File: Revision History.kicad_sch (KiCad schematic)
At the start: 0 parts

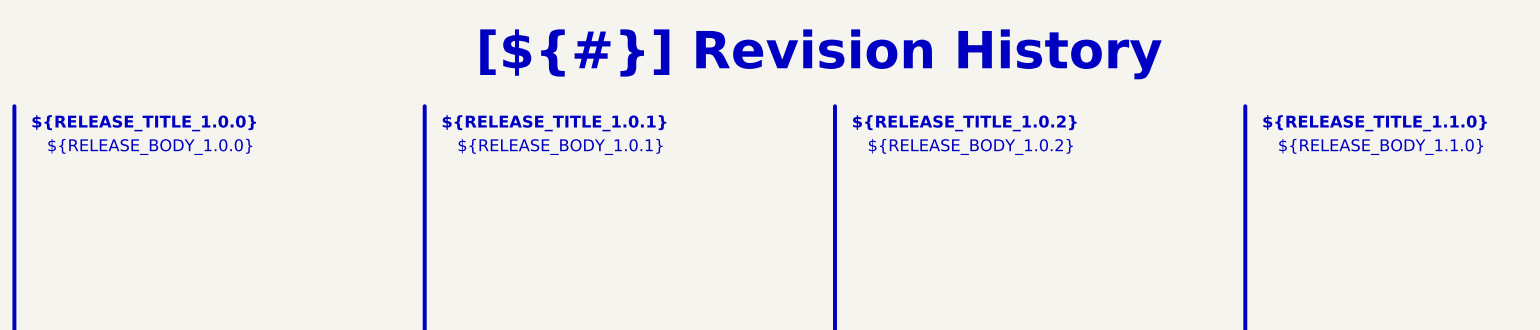
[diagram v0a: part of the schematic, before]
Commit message: Fill template pages: block diagram, power sequencing, cover notes, architecture
- Block Diagram redrawn from the real design: phase path (MR60PW, shunts),
  current and voltage channels with their gains and bandwidths, AD7606C-18,
  power chain, target specifications
- Power - Sequencing: start-up curves taken from the LTspice simulations
  (boost soft-start, analog rails) and rail table with sources, levels
  and timings
- Cover page: real design notes instead of the template examples
- Project Architecture: power-supply block documented, contiguous page
  numbers (Power Supply is page 6)
- Revision History: one column fed by the [Unreleased] changelog section
- sheet titles shortened so they fit the cover-page index: INA241 - Phase
  Sensing, Power Supply - Analog Rails

Sheet-level polylines carry no fill attribute (KiBot schematic reader).

Co-Authored-By: Claude Opus 5.5 <noreply@anthropic.com>
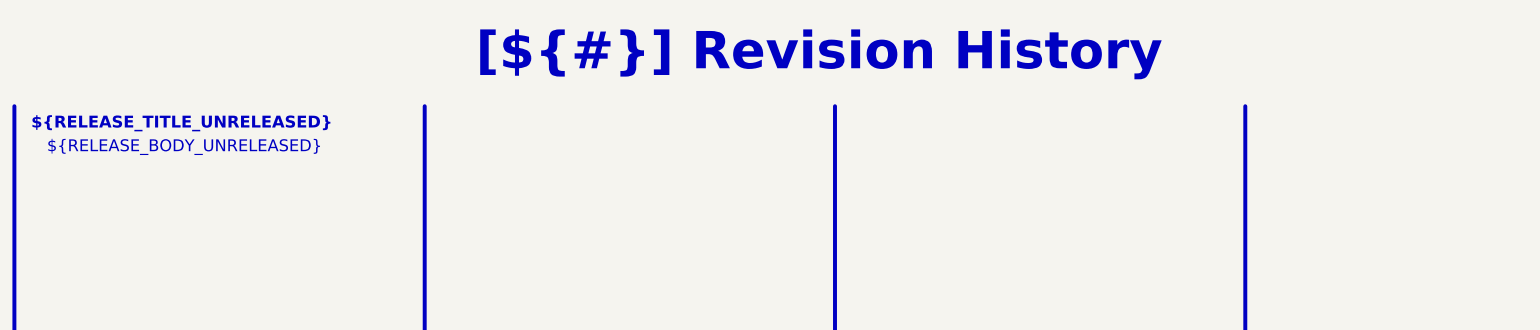
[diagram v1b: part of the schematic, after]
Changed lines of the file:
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@@
 		(company "${COMPANY}")
-	)
-	(text_box "${RELEASE_BODY_1.1.0}"
-		(exclude_from_sim no)
-		(at 220.98 35.56 0)
-		(size 58.42 111.76)
-		(margins 1.4287 1.4287 1.4287 1.4287)
-		(stroke
-			(width -0.0001)
-			(type default)
-		)
-		(fill
-			(type none)
-		)
-		(effects
-			(font
-				(face "Arial")
-				(size 1.905 1.905)
-				(color 0 0 0 1)
-			)
-			(justify left top)
-		)
 	)
 	(text_box "[${#}] ${TITLE}"
@@
 		)
 	)
-	(text_box "${RELEASE_BODY_1.0.0}"
+	(text_box "${RELEASE_BODY_UNRELEASED}"
 		(exclude_from_sim no)
 		(at 22.86 35.56 0)
@@
 		)
 	)
-	(text_box "${RELEASE_TITLE_1.0.2}"
-		(exclude_from_sim no)
-		(at 152.4 31.75 0)
-		(size 57.15 7.62)
-		(margins 1.4287 1.4287 1.4287 1.4287)
-		(stroke
-			(width -0.0001)
-			(type default)
-		)
-		(fill
-			(type none)
-		)
-		(effects
-			(font
-				(face "Arial")
-				(size 1.905 1.905)
-				(thickness 0.254)
-				(bold yes)
-			)
-			(justify left top)
-		)
-	)
-	(text_box "${RELEASE_BODY_1.0.2}"
-		(exclude_from_sim no)
-		(at 154.94 35.56 0)
-		(size 58.42 111.76)
-		(margins 1.4287 1.4287 1.4287 1.4287)
-		(stroke
-			(width -0.0001)
-			(type default)
-		)
-		(fill
-			(type none)
-		)
-		(effects
-			(font
-				(face "Arial")
-				(size 1.905 1.905)
-				(color 0 0 0 1)
-			)
-			(justify left top)
-		)
-	)
-	(text_box "${RELEASE_BODY_1.0.1}"
-		(exclude_from_sim no)
-		(at 88.9 35.56 0)
-		(size 57.15 105.41)
-		(margins 1.4287 1.4287 1.4287 1.4287)
-		(stroke
-			(width -0.0001)
-			(type default)
-		)
-		(fill
-			(type none)
-		)
-		(effects
-			(font
-				(face "Arial")
-				(size 1.905 1.905)
-				(color 0 0 0 1)
-			)
-			(justify left top)
-		)
-	)
-	(text_box "${RELEASE_TITLE_1.0.0}"
+	(text_box "${RELEASE_TITLE_UNRELEASED}"
 		(exclude_from_sim no)
 		(at 20.32 31.75 0)
 		(size 57.15 7.62)
 		(margins 1.4287 1.4287 1.4287 1.4287)
-		(stroke
-			(width -0.0001)
-			(type default)
-		)
-		(fill
-			(type none)
-		)
-		(effects
-			(font
-				(face "Arial")
-				(size 1.905 1.905)
-				(thickness 0.254)
-				(bold yes)
-			)
-			(justify left top)
-		)
-	)
-	(text_box "${RELEASE_TITLE_1.0.1}"
-		(exclude_from_sim no)
-		(at 86.36 31.75 0)
-		(size 57.15 7.62)
-		(margins 1.4287 1.4287 1.4287 1.4287)
-		(stroke
-			(width -0.0001)
-			(type default)
-		)
-		(fill
-			(type none)
-		)
-		(effects
-			(font
-				(face "Arial")
-				(size 1.905 1.905)
-				(thickness 0.254)
-				(bold yes)
-			)
-			(justify left top)
-		)
-	)
-	(text_box "${RELEASE_TITLE_1.1.0}"
-		(exclude_from_sim no)
-		(at 218.44 31.75 0)
-		(size 57.15 7.62)
-		(margins 1.4287 1.4287 1.4287 1.4287)

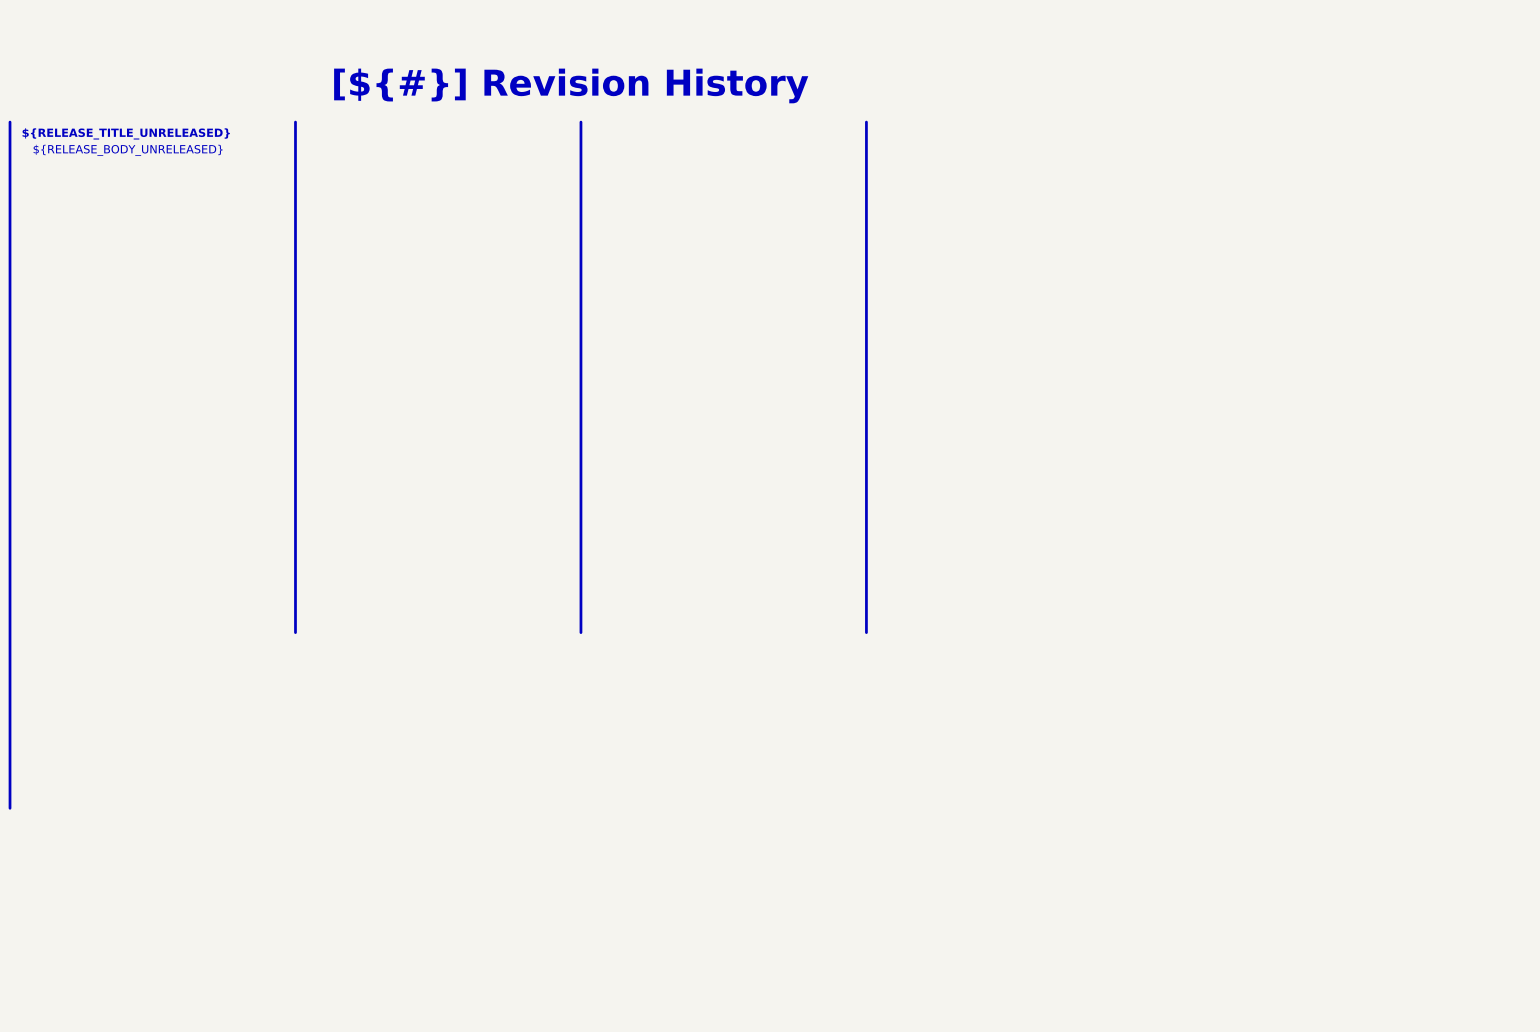
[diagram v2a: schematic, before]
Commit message: Restyle schematic sheets, new title block logo, WE-MAPI inductor in simulations
- Schematic sheets: restyled frames, tables and text boxes
- Title block: INGENIERIE FRANCE logo in KDT_Template_GIT.kicad_wks
- LTspice: L1 modelled as WE-MAPI 4030 74438357022 (22 mOhm),
  simulations 01 and 03 rerun, README and results updated

Co-Authored-By: Claude Opus 5.5 <noreply@anthropic.com>
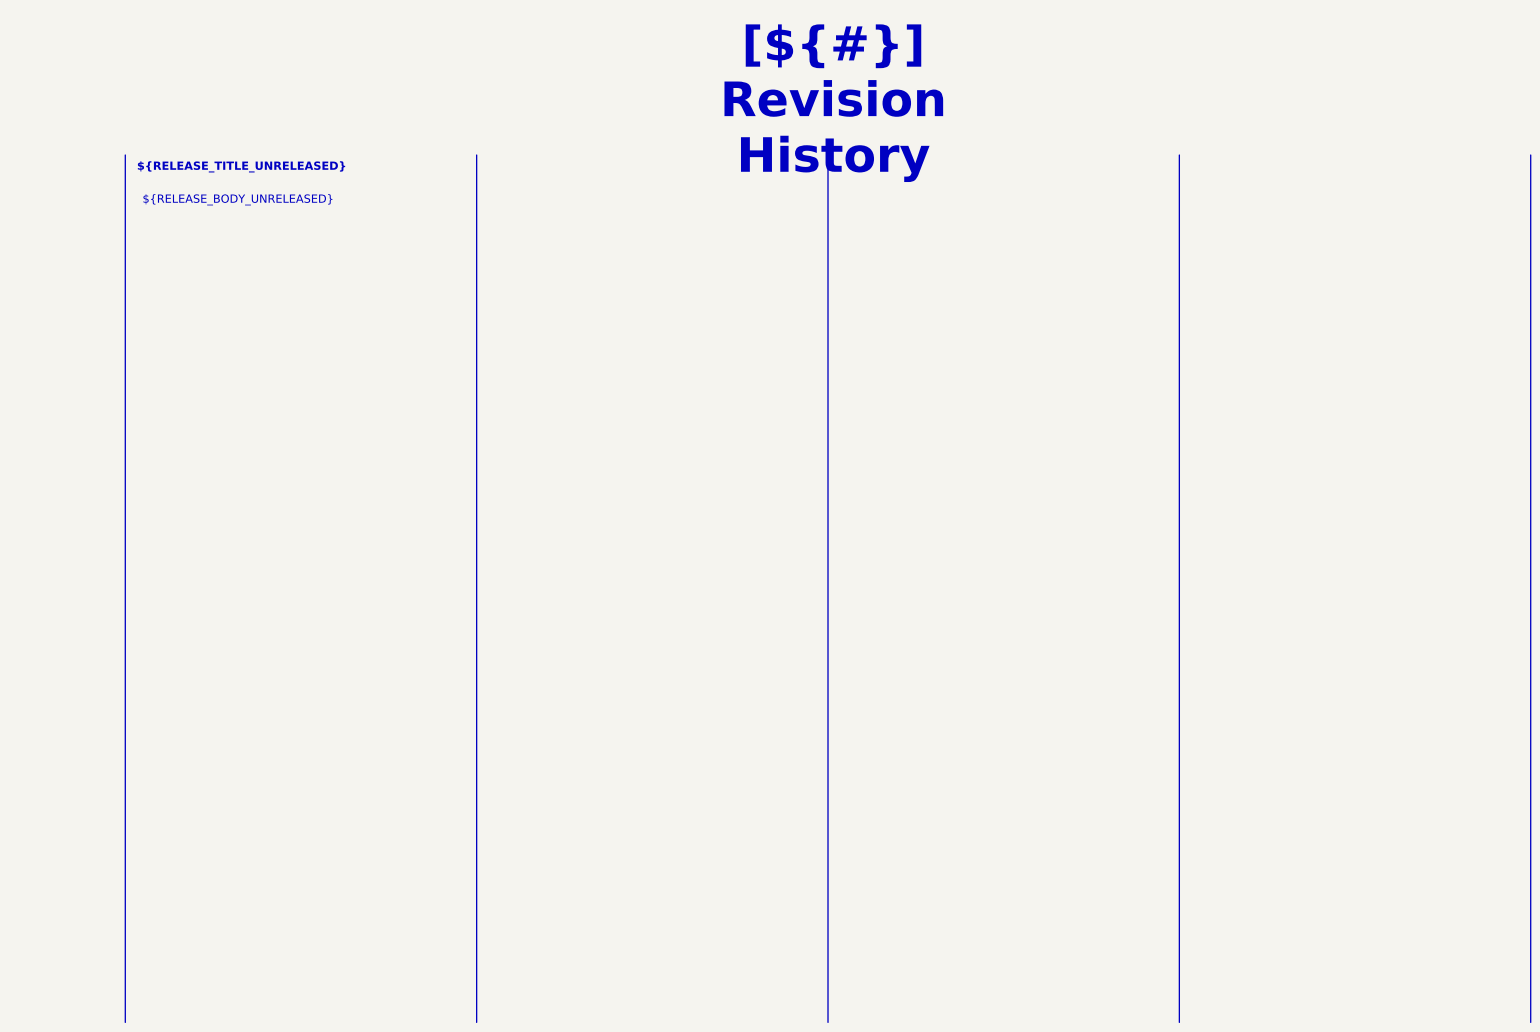
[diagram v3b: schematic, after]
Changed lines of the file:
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@@
 	(generator "eeschema")
 	(generator_version "10.0")
-	(paper "A4")
+	(paper "A3")
 	(title_block
 		(title "Revision History")
@@
 		(company "${COMPANY}")
 	)
-	(text_box "[${#}] ${TITLE}"
+(text_box "[${#}] ${TITLE}"
 		(exclude_from_sim no)
-		(at 80.01 16.51 0)
-		(size 137.16 12.7)
-		(margins 4.4999 4.4999 4.4999 4.4999)
+		(at 161.29 20.32 0)
+		(size 96.52 12.7)
+		(margins 5.9999 5.9999 5.9999 5.9999)
 		(stroke
 			(width -0.0001)
@@
 			(font
 				(face "Times New Roman")
-				(size 6 6)
+				(size 8 8)
 				(thickness 1.2)
 				(bold yes)
@@
 	(text_box "${RELEASE_BODY_UNRELEASED}"
 		(exclude_from_sim no)
-		(at 22.86 35.56 0)
-		(size 58.42 146.05)
+		(at 48.26 46.99 0)
+		(size 76.2 191.77)
 		(margins 1.4287 1.4287 1.4287 1.4287)
 		(stroke
@@
 	(text_box "${RELEASE_TITLE_UNRELEASED}"
 		(exclude_from_sim no)
-		(at 20.32 31.75 0)
-		(size 57.15 7.62)
+		(at 46.99 39.37 0)
+		(size 78.74 6.35)
 		(margins 1.4287 1.4287 1.4287 1.4287)
 		(stroke
@@
 		)
 		(fill
-			(type none)
+			(type color)
+			(color 162 22 34 1)
 		)
 		(effects
@@
 				(thickness 0.254)
 				(bold yes)
+				(color 255 255 255 1)
 			)
 			(justify left top)
@@
 	(polyline
 		(pts
-			(xy 85.09 31.75) (xy 85.09 149.86)
+			(xy 45.72 39.37) (xy 45.72 240.03)
 		)
 		(stroke
-			(width 0.635)
-			(type default)
-			(color 0 0 0 1)
+			(width 0.3)
+			(type solid)
+			(color 190 190 190 1)
 		)
 	)
 	(polyline
 		(pts
-			(xy 151.13 31.75) (xy 151.13 149.86)
+			(xy 127 39.37) (xy 127 240.03)
 		)
 		(stroke
-			(width 0.635)
-			(type default)
-			(color 0 0 0 1)
+			(width 0.3)
+			(type solid)
+			(color 190 190 190 1)
 		)
 	)
 	(polyline
 		(pts
-			(xy 19.05 31.75) (xy 19.05 190.5)
+			(xy 208.28 39.37) (xy 208.28 240.03)
 		)
 		(stroke
-			(width 0.635)
-			(type default)
-			(color 0 0 0 1)
+			(width 0.3)
+			(type solid)
+			(color 190 190 190 1)
 		)
 	)
 	(polyline
 		(pts
-			(xy 217.17 31.75) (xy 217.17 149.86)
+			(xy 289.56 39.37) (xy 289.56 240.03)
 		)
 		(stroke
-			(width 0.635)
-			(type default)
-			(color 0 0 0 1)
+			(width 0.3)
+			(type solid)
+			(color 190 190 190 1)
 		)
 	)
+	(polyline
+		(pts
+			(xy 370.84 39.37) (xy 370.84 240.03)
+		)
+		(stroke
+			(width 0.3)
+			(type solid)
+			(color 190 190 190 1)
+		)
+	)
